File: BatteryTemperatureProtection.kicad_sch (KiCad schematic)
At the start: 8 parts, among them Q1 SIRA99DP-T1-GE3, Q2 IRLML2803

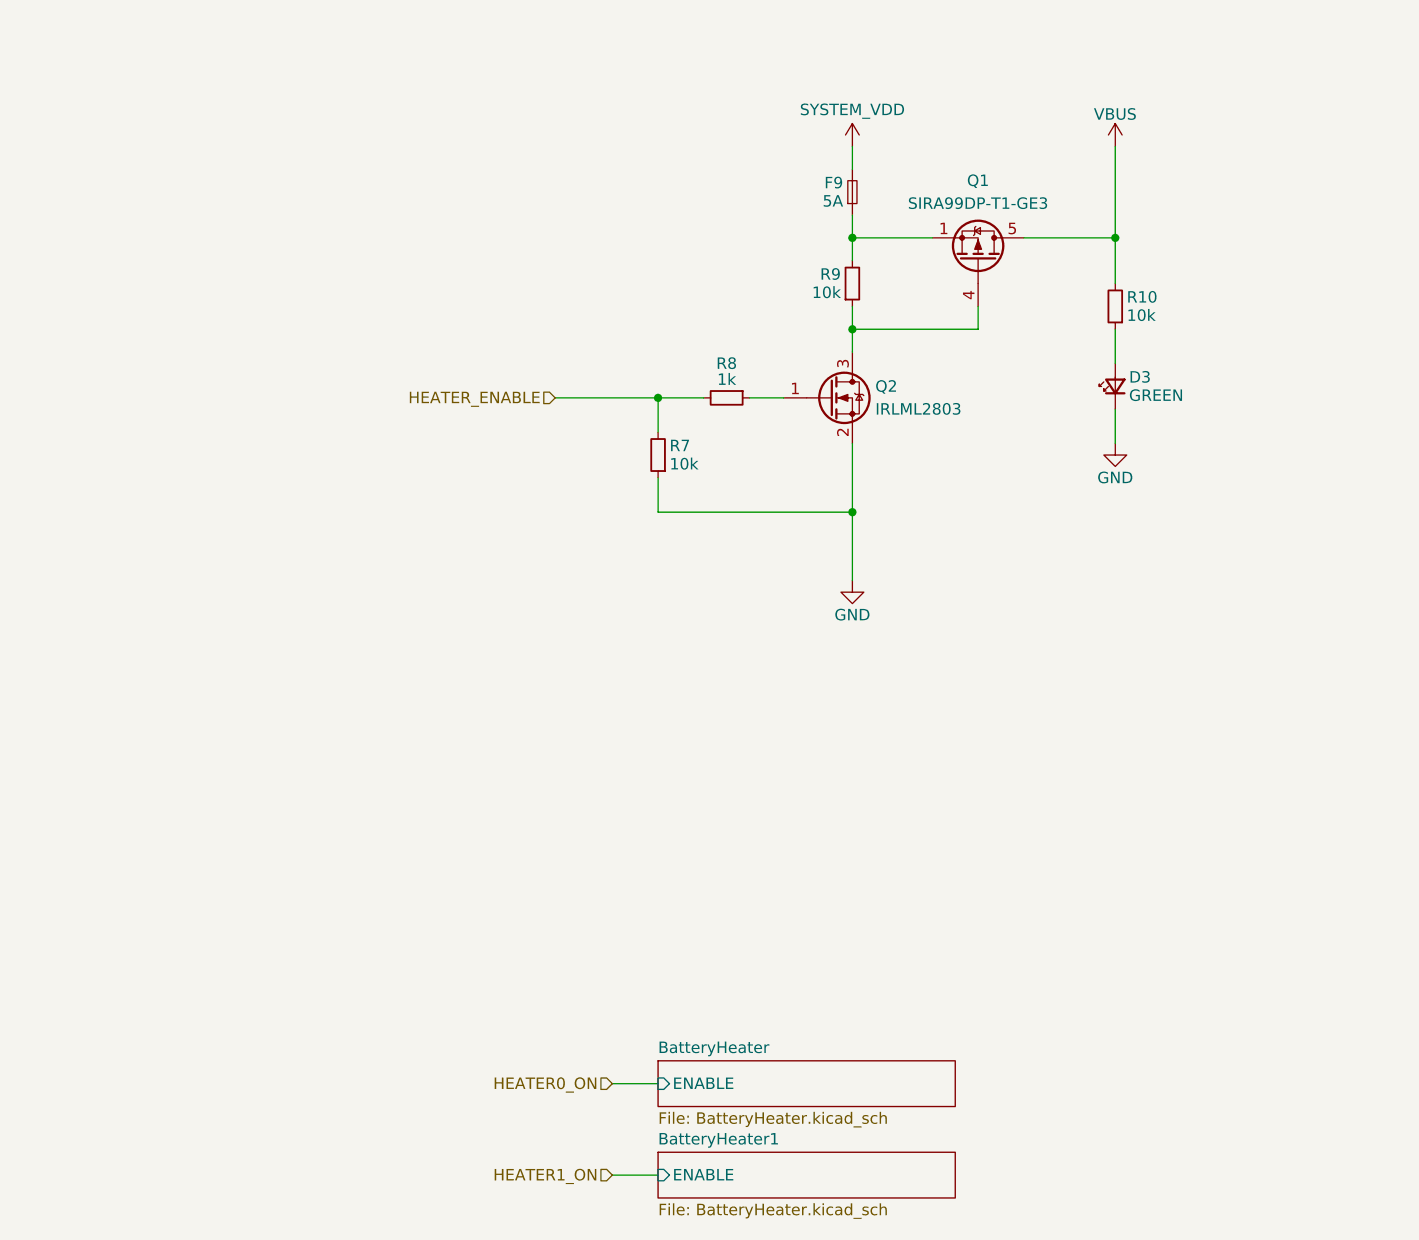
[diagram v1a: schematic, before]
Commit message: Added Schmitt Trigger mode for heaters
In the event that the mcu goes down, the thermistors will now be ale to control the heaters independently.
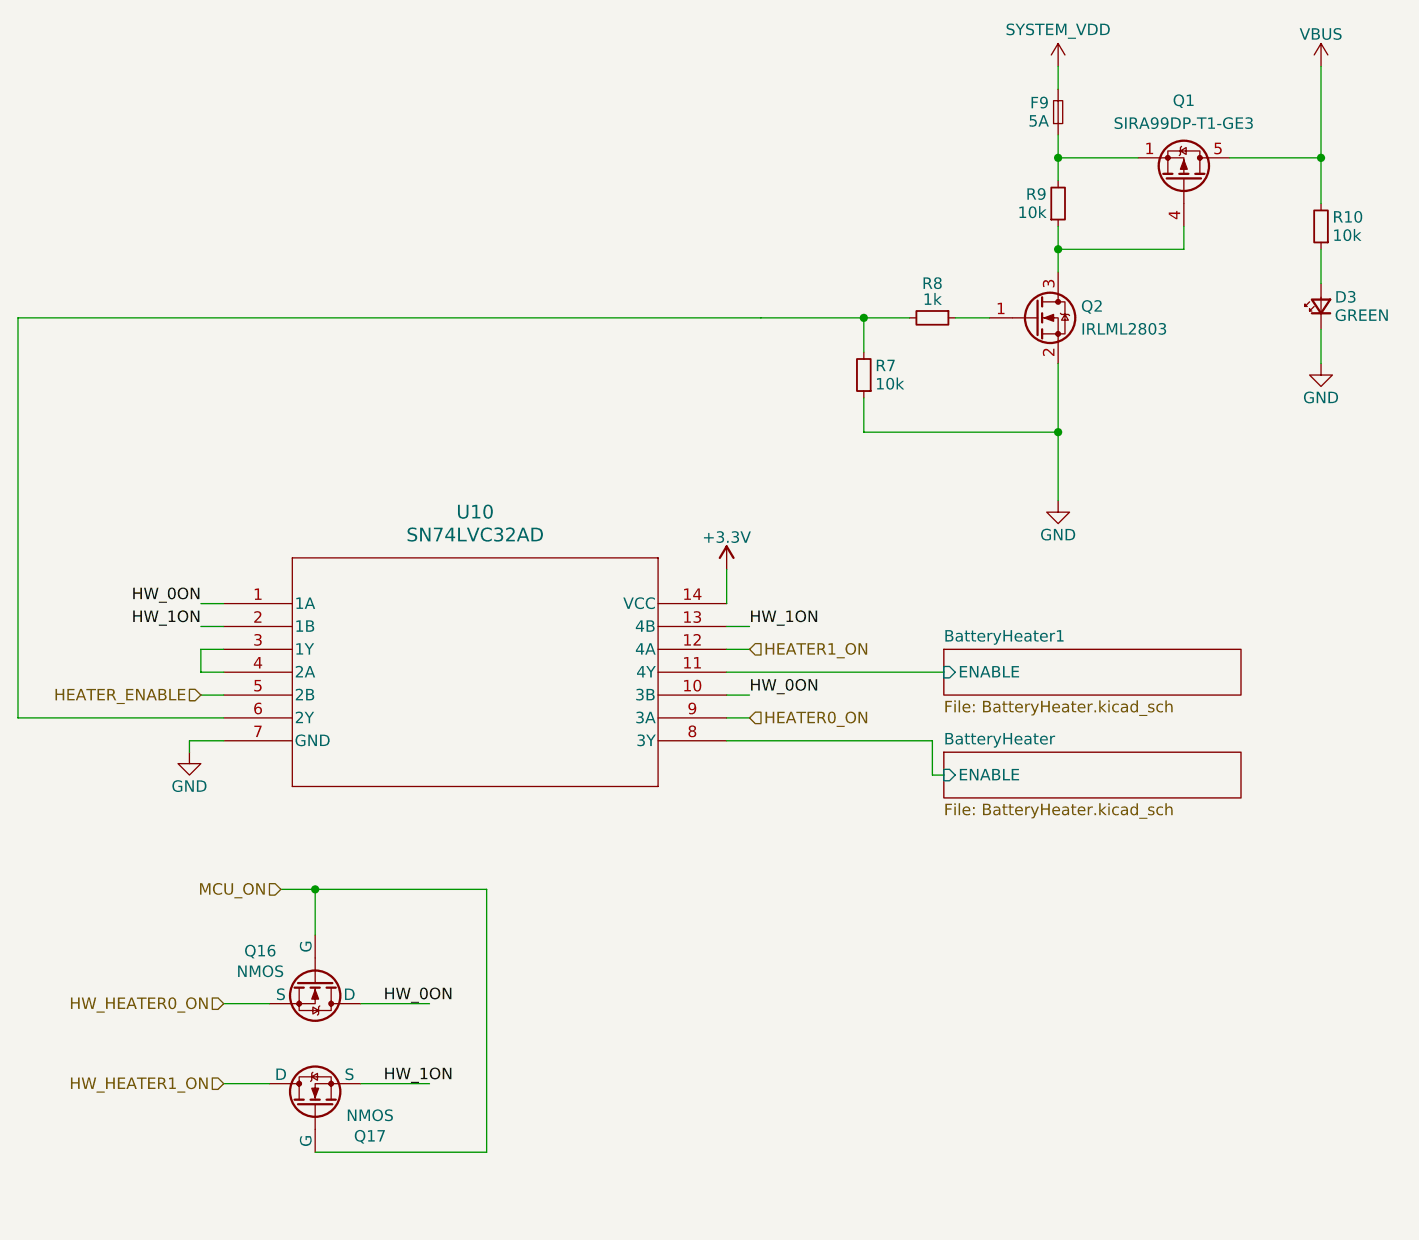
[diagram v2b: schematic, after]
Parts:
- added Q16, Q17: NMOS, symbol Simulation_SPICE:NMOS
- added U10: SN74LVC32AD, D14, symbol SN74LVC32AD:SN74LVC32AD
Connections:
- net GND: now also U10.7 (GND)
- net HEATER0_ON: now also U10.9 (3A)
- net HEATER1_ON: now also U10.12 (4A)
- net HEATER_ENABLE: now also U10.5 (2B); no longer R7.2, R8.2
- new net: U10.3 (1Y), U10.4 (2A)
- new net: R7.2, R8.2, U10.6 (2Y)
- new net +3.3V: U10.14 (VCC)
- new net BatteryHeater/ENABLE: U10.8 (3Y)
- new net BatteryHeater1/ENABLE: U10.11 (4Y)
- new net HW_0ON: Q16.1 (D), U10.1 (1A), U10.10 (3B)
- new net HW_1ON: Q17.3 (S), U10.13 (4B), U10.2 (1B)
- new net HW_HEATER0_ON: Q16.3 (S)
- new net HW_HEATER1_ON: Q17.1 (D)
- new net MCU_ON: Q16.2 (G), Q17.2 (G)
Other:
- moved on the sheet: D3, F9, Q1, Q2, R10, R7, R8, R9

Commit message: Layout in progress
In the middle of completing layout
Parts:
- added R76, R77: 10k, Resistor_SMD:R_0603_1608Metric, symbol Device:R_Small
- Q16, Q17: value NMOS -> IRLML2803; footprint (none) -> Package_TO_SOT_SMD:SOT-23
- U10: footprint D14 -> Argus-Misc:D14
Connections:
- net GND: now also R76.1, R77.1
- net HW_0ON: now also R76.2
- net HW_1ON: now also R77.2
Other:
- moved on the sheet: Q16
